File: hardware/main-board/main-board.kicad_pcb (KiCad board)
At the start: 2 copper layers, 176 x 55 mm, 101 parts, among them J1 BARREL_JACK, J2 CONN_01X10, J3 CONN_01X10, J4 USB_OTG, J5 CONN_02X05, J6 SMA, Q1 DDTD113ZC, Q2 DDTD113ZC, Q3 DDTD113ZC, Q4 DDTD113ZC, Q5 DDTD113ZC, Q6 FDB14N30TM, Q7 DDTD113ZC, Q8 DDTD113ZC, Q9 DDTD113ZC, SW1 SW_Push, SW2 SW_Push, SW3 SW_Push, SW4 SW_Push, U1 LD1117S33TR, U2 MAX1771, U3 STM32F302C, U4 FGPMMOPA6H, Y1 8MHz, Y2 32.768kHz

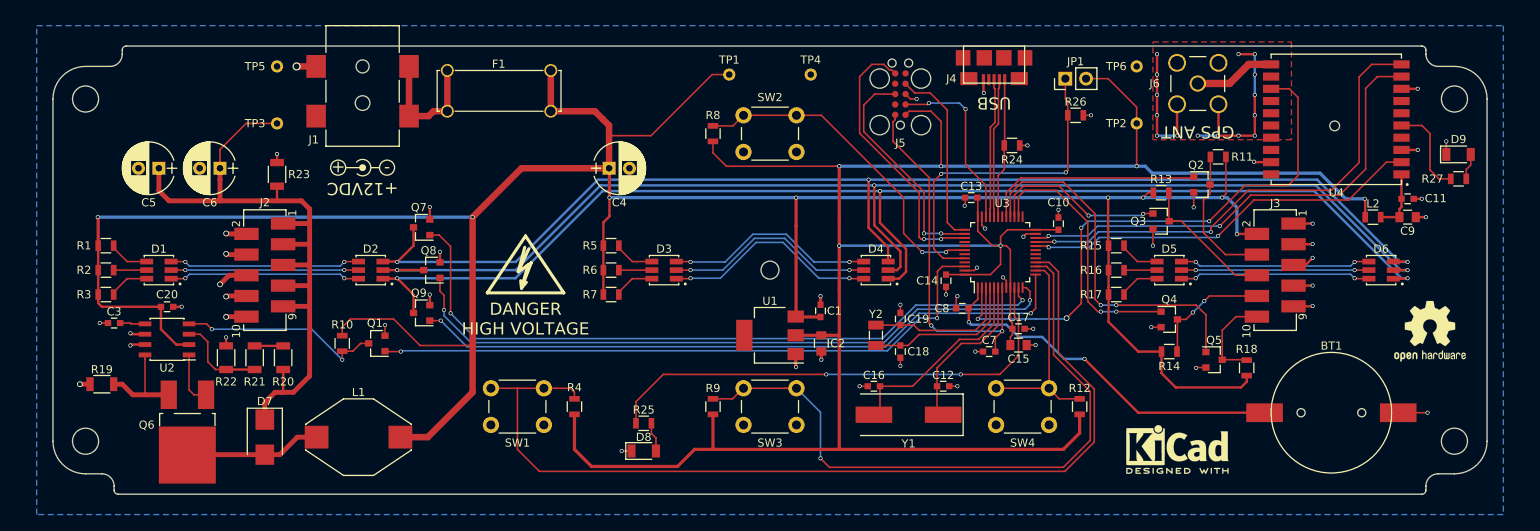
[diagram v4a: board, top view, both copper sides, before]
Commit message: Using DIP switch for BOOT mode.  Minor layout changes
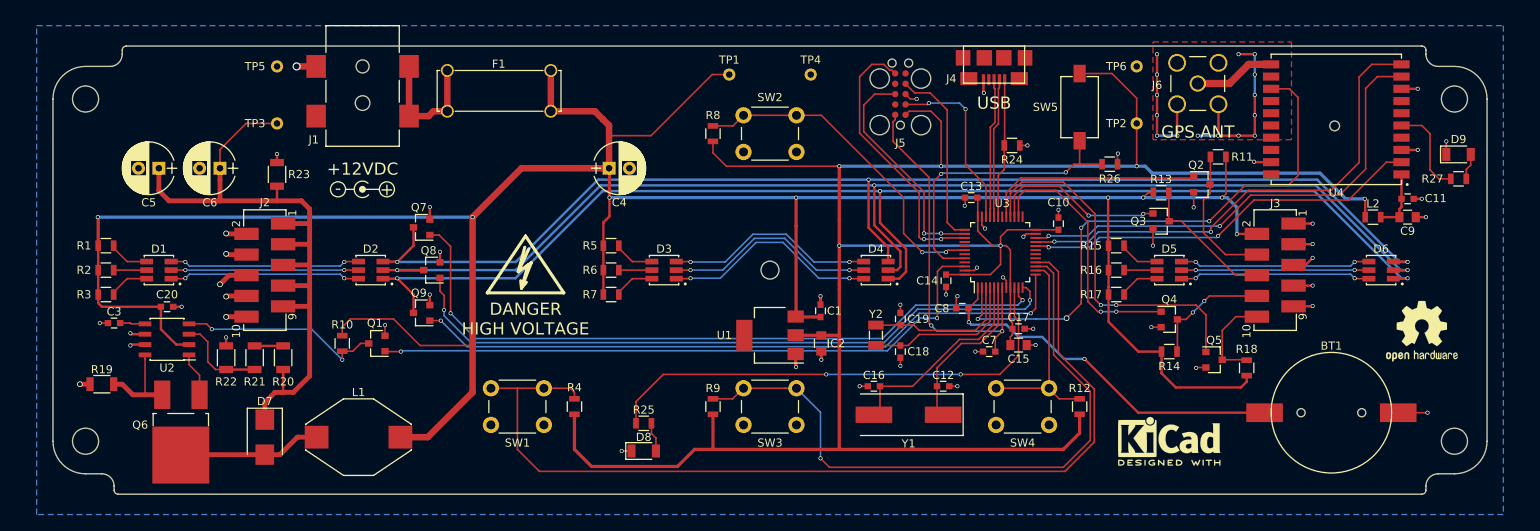
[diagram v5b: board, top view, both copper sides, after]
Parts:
- removed JP1: Jumper_NO_Small, Pin_Headers:Pin_Header_Straight_1x02_Pitch2.54mm
- added SW5: SW_DIP_x01, radio-clock:SDA01H1SBD, F.Cu at (188.0, 70.0)
- moved R26 7.32 mm to (191.7, 77.0)
- moved REF** 2.51 mm to (100.0, 80.0), turned to 0 degrees
- moved REF*** 1.41 mm to (199.0, 111.0)
- moved REF*** 1.00 mm to (230.0, 97.5)
- moved Q6 0.80 mm to (77.7, 109.0)
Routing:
- net /BOOT0: track 41.0 -> 37.0 mm
- net +3V3: track 285.9 -> 287.6 mm
- net Net-(Q6-Pad1): track 6.63 -> 5.43 mm
- net Net-(D7-Pad2): track 16.8 -> 17.6 mm
- net Net-(Q6-Pad3): track 12.2 -> 11.4 mm

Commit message: Final tweaks before board submission
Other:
- board text added: "12VDC"
- board text removed: "+12VDC"
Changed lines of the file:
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@@
     (links 233)
     (no_connects 5)
-    (area 54.657143 54.823809 245.342858 120.000001)
+    (area 61.924999 62.424999 238.075001 117.575001)
     (thickness 1.6)
     (drawings 34)
@@
   (gr_line (start 66 115) (end 68 115) (layer Edge.Cuts) (width 0.15))
   (gr_line (start 66 65) (end 69 65) (layer Edge.Cuts) (width 0.15))
-  (gr_text +12VDC (at 100 77.6) (layer F.SilkS)
+  (gr_text 12VDC (at 100 77.6) (layer F.SilkS)
     (effects (font (size 1.5 1.5) (thickness 0.3)))
   )
